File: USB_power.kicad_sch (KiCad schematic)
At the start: 16 parts, among them J1 JST-4-pin, J2 JST-2-pin, U1 BQ24074RGTR, U2 AP2127K-3.0TRG1

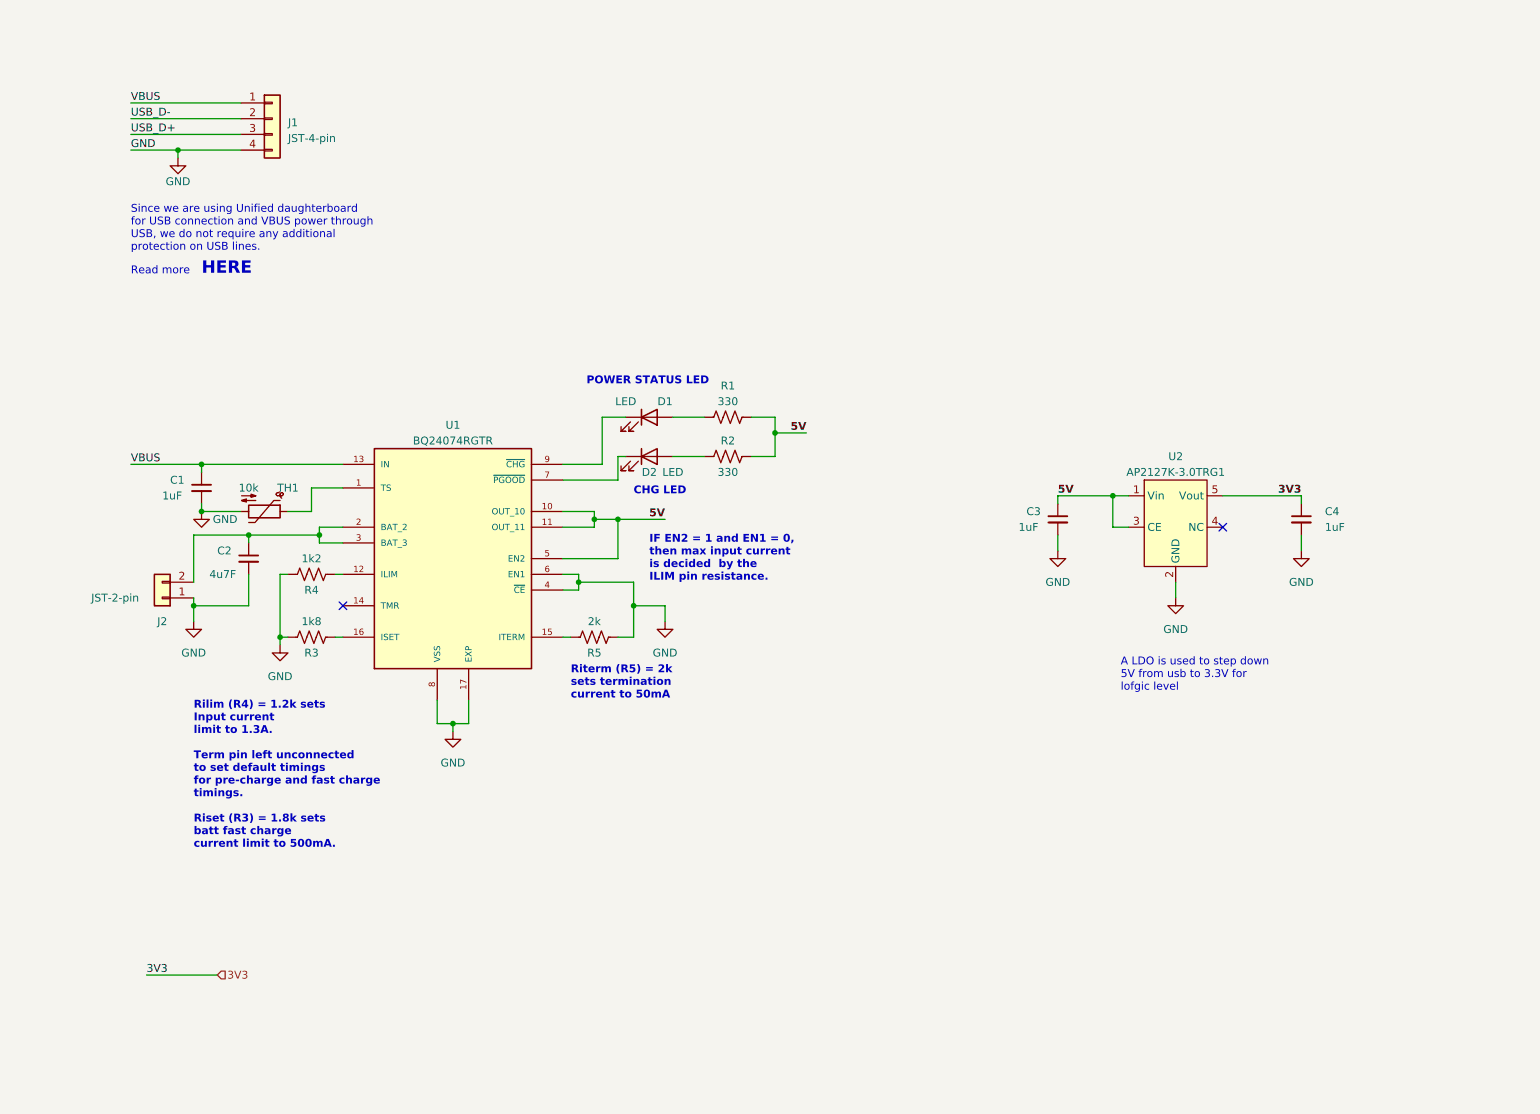
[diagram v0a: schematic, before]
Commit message: added seitch matrix to schematic
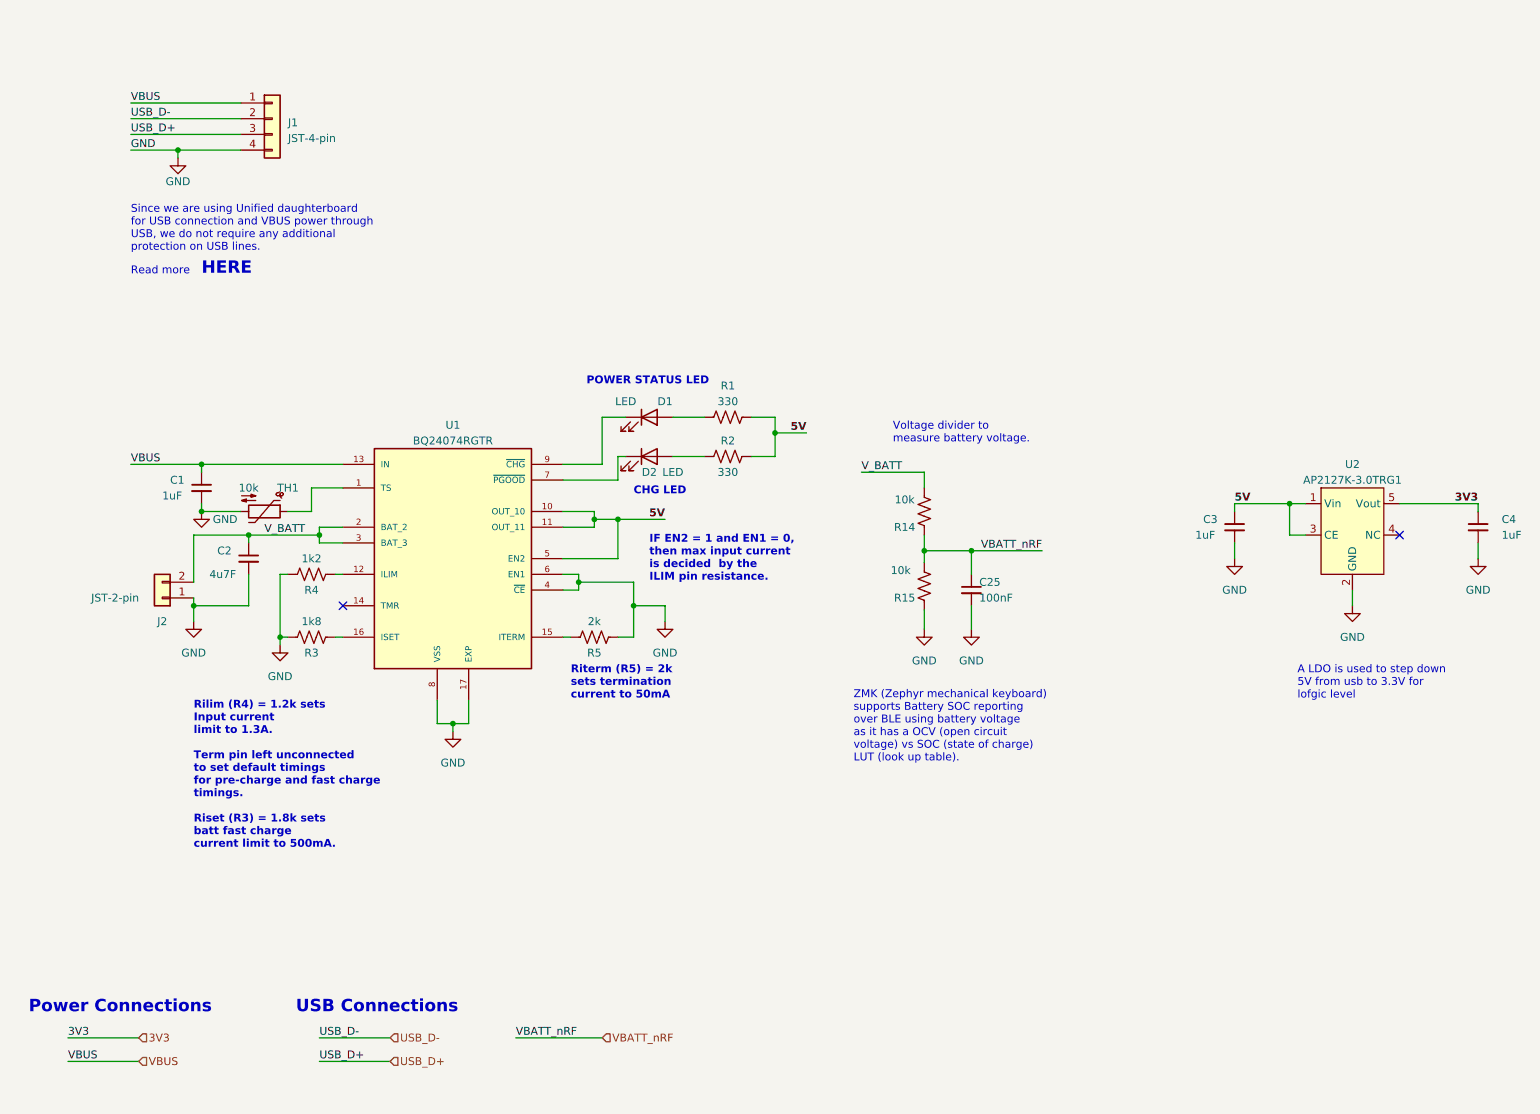
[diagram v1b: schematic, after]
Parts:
- added C25: 100nF, symbol keyboard:C_Small
- added R14, R15: 10k, symbol keyboard:R_US
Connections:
- net GND: now also C25.2, R15.1
- net V_BATT: now reaches C2.1, J2.2 (Pin_2), U1.2 (BAT_2), U1.3 (BAT_3)
- net V_BATT: now also R14.2
- new net VBATT_nRF: C25.1, R14.1, R15.2
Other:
- note added: "Power Connections"
- note added: "USB Connections"
- note added: "Voltage divider to measure battery voltage."
- note added: "ZMK (Zephyr mechanical keyboard) supports Battery SOC reporting over BLE using battery voltage as it has a OCV (open circuit voltage) vs SOC (state of charge) LUT (look up table)."
- moved on the sheet: C3, C4, U2

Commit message: Added 3d models to footprints and updated partnumbers
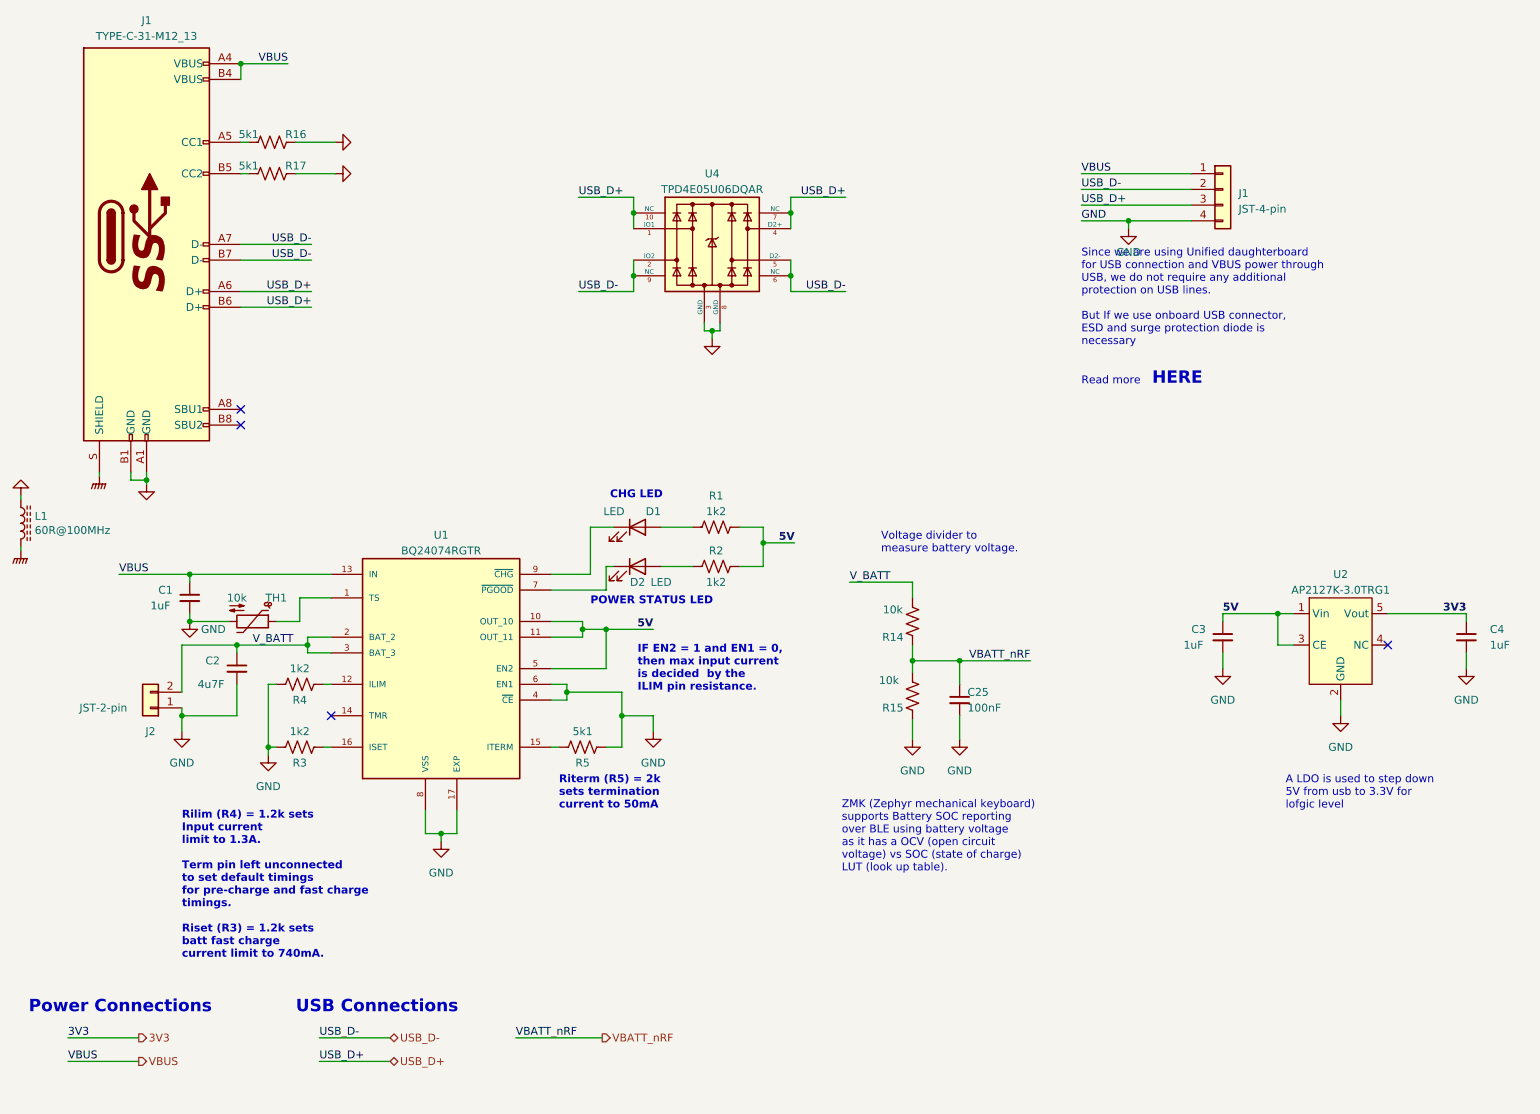
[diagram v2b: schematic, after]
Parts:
- added J1: TYPE-C-31-M12_13, keyboard:tyye_c_connector, symbol Unified-Daughterboard-rescue:TYPE-C-31-M12_13-acheronSymbols
- added L1: 60R@100MHz, Inductor_SMD:L_1206_3216Metric, symbol Unified-Daughterboard-rescue:L_Core_Ferrite-Device
- added R16, R17: 5k1, keyboard:R_0402_1005Metric, symbol keyboard:R_US
- added U4: TPD4E05U06DQAR, keyboard:USON-10, symbol keyboard:USB-protection-diode
- C1, C3, C4: footprint (none) -> keyboard:C_0603_1608Metric; LCSC PN 0603B105K250NT -> (none); LCSC Part Number (none) -> C1592; LCSC link https://www.lcsc.com/product-detail/Multilayer-Ceramic-Capacitors-MLCC-SMD-SMT_FH-Guangdong-Fenghua-Advanced-Tech-0603B105K250NT_C59302.html -> https://www.lcsc.com/product-detail/Multilayer-Ceramic-Capacitors-MLCC-SMD-SMT_Samsung-Electro-Mechanics-CL10A105KO8NNNC_C1592.html; PN (none) -> CL10A105KO8NNNC
- C2: footprint (none) -> keyboard:C_0805_2012Metric; LCSC PN 0603B105K250NT -> (none); LCSC Part Number (none) -> C1779; LCSC link https://www.lcsc.com/product-detail/Multilayer-Ceramic-Capacitors-MLCC-SMD-SMT_FH-Guangdong-Fenghua-Advanced-Tech-0603B105K250NT_C59302.html -> https://www.lcsc.com/product-detail/Multilayer-Ceramic-Capacitors-MLCC-SMD-SMT_Samsung-Electro-Mechanics-CL21A475KAQNNNE_C1779.html; PN (none) -> CL21A475KAQNNNE
- C25: footprint (none) -> keyboard:C_0402_1005Metric; LCSC Part Number (none) -> C1525; LCSC link (none) -> https://www.lcsc.com/product-detail/Multilayer-Ceramic-Capa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; PN (none) -> CL05B104KO5NNNC
- D1: footprint (none) -> keyboard:LED_0603_1608Metric; LCSC PN C2904374 -> (none); LCSC Part Number (none) -> C965799; LCSC link (none) -> https://www.lcsc.com/product-detail/Light-Emitting-Diodes-L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; PN (none) -> XL-1608SURC-06
- D2: LCSC PN C193191 -> (none); LCSC Part Number (none) -> C193191; LCSC link (none) -> https://www.lcsc.com/product-detail/Light-Emitting-Diodes-L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; PN (none) -> ORH-B36G
- J1: LCSC PN C160404 -> (none); PN (none) -> SM04B-SRSS-TB(LF)(SN)
- J2: footprint (none) -> keyboard:JST-2-pin; LCSC PN C160402 -> (none); PN (none) -> SM02B-SRSS-TB(LF)(SN)
- R1, R2: value 330 -> 1k2; footprint (none) -> keyboard:R_0402_1005Metric; LCSC Part Number (none) -> C138040; LCSC link (none) -> https://www.lcsc.com/product-detail/Chip-Resistor-Surface-M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; PN (none) -> RC0402FR-071K2L
- R14, R15: footprint (none) -> keyboard:R_0402_1005Metric; LCSC Part Number (none) -> C60490; LCSC link (none) -> https://www.lcsc.com/product-detail/Chip-Resistor-Surface-M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; PN (none) -> RC0402FR-0710KL
- R3: value 1k8 -> 1k2; footprint (none) -> keyboard:R_0402_1005Metric; LCSC Part Number (none) -> C138040; LCSC link (none) -> https://www.lcsc.com/product-detail/Chip-Resistor-Surface-M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; PN (none) -> RC0402FR-071K2L
- R4: footprint (none) -> keyboard:R_0402_1005Metric; LCSC Part Number (none) -> C138040; LCSC link (none) -> https://www.lcsc.com/product-detail/Chip-Resistor-Surface-M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; PN (none) -> RC0402FR-071K2L
- R5: value 2k -> 5k1; footprint (none) -> keyboard:R_0402_1005Metric; LCSC Part Number (none) -> C105872; LCSC link (none) -> https://www.lcsc.com/product-detail/Chip-Resistor-Surface-M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; PN (none) -> RC0402FR-075K1L
- TH1: footprint (none) -> keyboard:R_0402_1005Metric; LCSC Part Number (none) -> C95939; LCSC link (none) -> https://www.lcsc.com/product-detail/span-style-background-c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; PN (none) -> SDNT1005X103F3950FTF
- U1: footprint QFN50P300X300X100-17N -> keyboard:QFN-16; LCSC PN BQ24074RGTR -> (none); MANUFACTURER Texas Instruments -> (none); MAXIMUM_PACKAGE_HIEGHT 1mm -> (none); PARTREV M -> (none); PN (none) -> BQ24074RGTR; STANDARD IPC 7351B -> (none)
- U2: footprint (none) -> keyboard:SOT-23-5; LCSC PN AP2125K-3.3TRG1 -> (none); LCSC link (none) -> https://www.lcsc.com/product-detail/Linear-Voltage-Regulato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; PN (none) -> AP2127K-3.0TRG1
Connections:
- net GND: now also J1.A1 (GND), J1.B1 (GND), L1.1, R16.2, R17.2, U4.3 (GND), U4.8 (GND)
- net USB_D+: now also J1.A6 (D+), J1.B6 (D+), U4.1 (IO1), U4.10 (NC), U4.4 (D2+), U4.7 (NC)
- net USB_D-: now also J1.A7 (D-), J1.B7 (D-), U4.2 (IO2), U4.5 (D2-), U4.6 (NC), U4.9 (NC)
- net VBUS: now also J1.A4 (VBUS), J1.B4 (VBUS)
- new net: J1.B5 (CC2), R17.1
- new net: J1.A5 (CC1), R16.1
- new net GNDPWR: J1.S (SHIELD), L1.2
- no-connect marks 2 -> 4
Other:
- note added: "Rilim (R4) = 1.2k sets Input current limit to 1.3A. Term pin left unconnected to set default timings for pre-charge and fast charge timings. Riset (R3) = 1.2k sets batt fast charge current limit to 740mA."
- note added: "Since we are using Unified daughterboard for USB connection and VBUS power through USB, we do not require any additional protection on USB lines. But If we use onboard USB connector, ESD and surge protection diode is necessary"
- note removed: "Rilim (R4) = 1.2k sets Input current limit to 1.3A. Term pin left unconnected to set default timings for pre-charge and fast charge timings. Riset (R3) = 1.8k sets batt fast charge current limit to 500mA."
- note removed: "Since we are using Unified daughterboard for USB connection and VBUS power through USB, we do not require any additional protection on USB lines."
- moved on the sheet: C1, C2, C25, C3, C4, D1, D2, J1, J2, R1, R14, R15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

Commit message: Pcb routing complete
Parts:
- removed J1: JST-4-pin, keyboard:JST-4-pin, symbol keyboard:JST-4-pin
- removed J2: JST-2-pin, keyboard:JST-2-pin, symbol keyboard:JST-2-pin
- added BT1: Lipo cell, keyboard:JST-2-pin, symbol keyboard:Battery_Cell
- L1: footprint Inductor_SMD:L_1206_3216Metric -> keyboard:L_0603_1608Metric
- U1: LCSC Part Number (none) -> C54313
- U2: LCSC Part Number (none) -> C460328
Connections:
- net GND: now also BT1.2 (-)
- net V_BATT: now also BT1.1 (+)
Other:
- note added: "USB bus protection TVS diode"
- note added: "USB-C connector"
- note removed: "HERE"
- note removed: "Read more"
- note removed: "Since we are using Unified daughterboard for USB connection and VBUS power through USB, we do not require any additional protection on USB lines. But If we use onboard USB connector, ESD and surge protection diode is necessary"
- moved on the sheet: C1, C2, D1, D2, J1, L1, R1, R16, R17, R2, R3, R4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

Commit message: Completed routing and solved DRC
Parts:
- added J1: JST-4-pin, keyboard:JST-4-pin, symbol keyboard:JST-4-pin
- added SW1: MK-12C02-G025, keyboard:SPDT, symbol keyboard:SW_SPDT
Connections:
- net 5V: now also SW1.1 (A)
- net GND: now also J1.4 (Pin_4)
- net USB_D+: now also J1.3 (Pin_3)
- net USB_D-: now also J1.2 (Pin_2)
- net VBUS: now also J1.1 (Pin_1), SW1.2 (B); no longer C1.1, U1.13 (IN)
- new net CHG_IN: C1.1, SW1.3 (C), U1.13 (IN)
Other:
- note added: "A SPDT switch is used to select power source. Switch position 1 - Direct power from USB connector. Switch position 2 - Power from battery and USB connector. If anybody wants to use keyboard without battery and cahrger module can do so by putting the switch in position 1. If battery is connected, then put it to position 2."
- note added: "HERE"
- note added: "This keyboard has a onboard USB-c Connector and also has support for universal daughterboard USB connectors. learn more about universal daughterboard"
- moved on the sheet: J1, L1, R16, R17, U4
